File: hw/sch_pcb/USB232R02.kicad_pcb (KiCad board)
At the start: 2 copper layers, 40.1 x 30 mm, 38 parts, among them J1 USB_B, J10 -, J11 -, J12 -, J13 -, J14 -, J15 -, J16 -, J17 HEADER_2x01_PARALLEL, J2 HEADER_2x03_PARALLEL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

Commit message: update submodule
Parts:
- H1, H2, H3, H4: moved to F.Cu
- turned H1 to 0 degrees
- turned H2 to 0 degrees
- turned H3 to 0 degrees
- turned H4 to 0 degrees

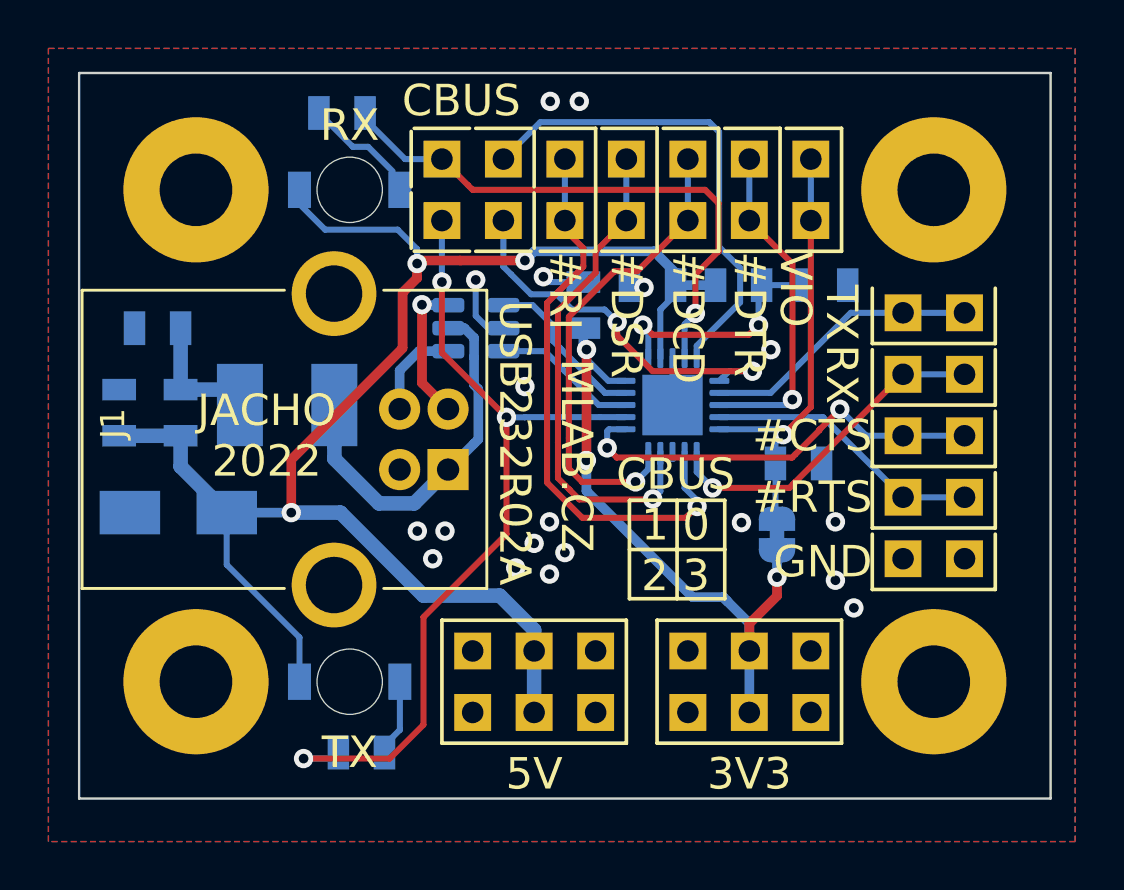
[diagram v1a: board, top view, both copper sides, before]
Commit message: clean repo, update kicad footprints, prepare to assembly
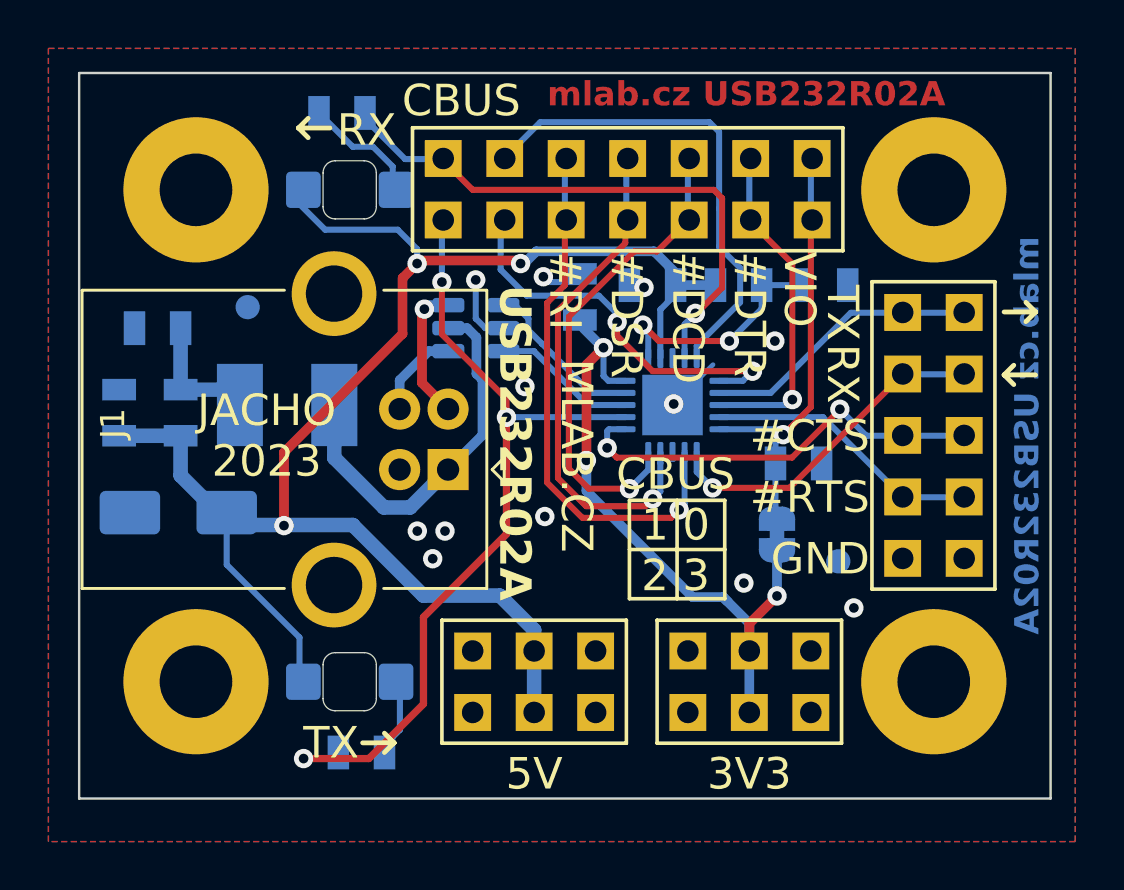
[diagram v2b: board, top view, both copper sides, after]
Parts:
- removed J10, J11, J12, J4, J9: -, Mlab_Pin_Headers:Straight_2x01
- removed J13, J14, J15, J16: -, Mlab_Pin_Headers:Straight_1x01
- removed J17, J5, J6, J7, J8: HEADER_2x01_PARALLEL, Mlab_Pin_Headers:Straight_2x01
- added FID1: Fiducial, Fiducial:Fiducial_1mm_Mask2mm, B.Cu at (160.2, 105.7)
- added FID2: Fiducial, Fiducial:Fiducial_1mm_Mask2mm, B.Cu at (135.8, 95.2)
- added J18: HEADER_2x07, Mlab_Pin_Headers:Straight_2x07, F.Cu at (151.5, 90.3)
- added J19: HEADER_2x05_PARALLEL, Mlab_Pin_Headers:Straight_2x05, F.Cu at (164.1, 100.5)
- D2, D3: footprint Mlab_D:LED_1206 -> Mlab_D:LED_1206_2
- J2, J3: value HEADER_2x03_PARALLEL -> HEADER_2x03
- moved C3 0.37 mm to (149.5, 94.8)
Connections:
- net /DM renamed /DN
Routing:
- net /#RI: track 23.8 -> 22.4 mm
- net /DN: track 6.92 -> 6.35 mm
- net /TXLED/CBUS2: track 35.3 -> 34.8 mm
- net GND: track 7.16 -> 7.40 mm, vias 19 -> 12
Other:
- rule pad_to_mask_clearance: 0.2 -> 0.1
- board text added: "JACHO 2023"
- board text added: "mlab.cz USB232R02A"
- board text removed: "JACHO 2022"
